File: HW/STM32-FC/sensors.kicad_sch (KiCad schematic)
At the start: 19 parts, among them J3 Molex 53048-03, U1 AMS1117-3.3, U5 BMP280, U7 BMI088, U8 LIS2MDLTR

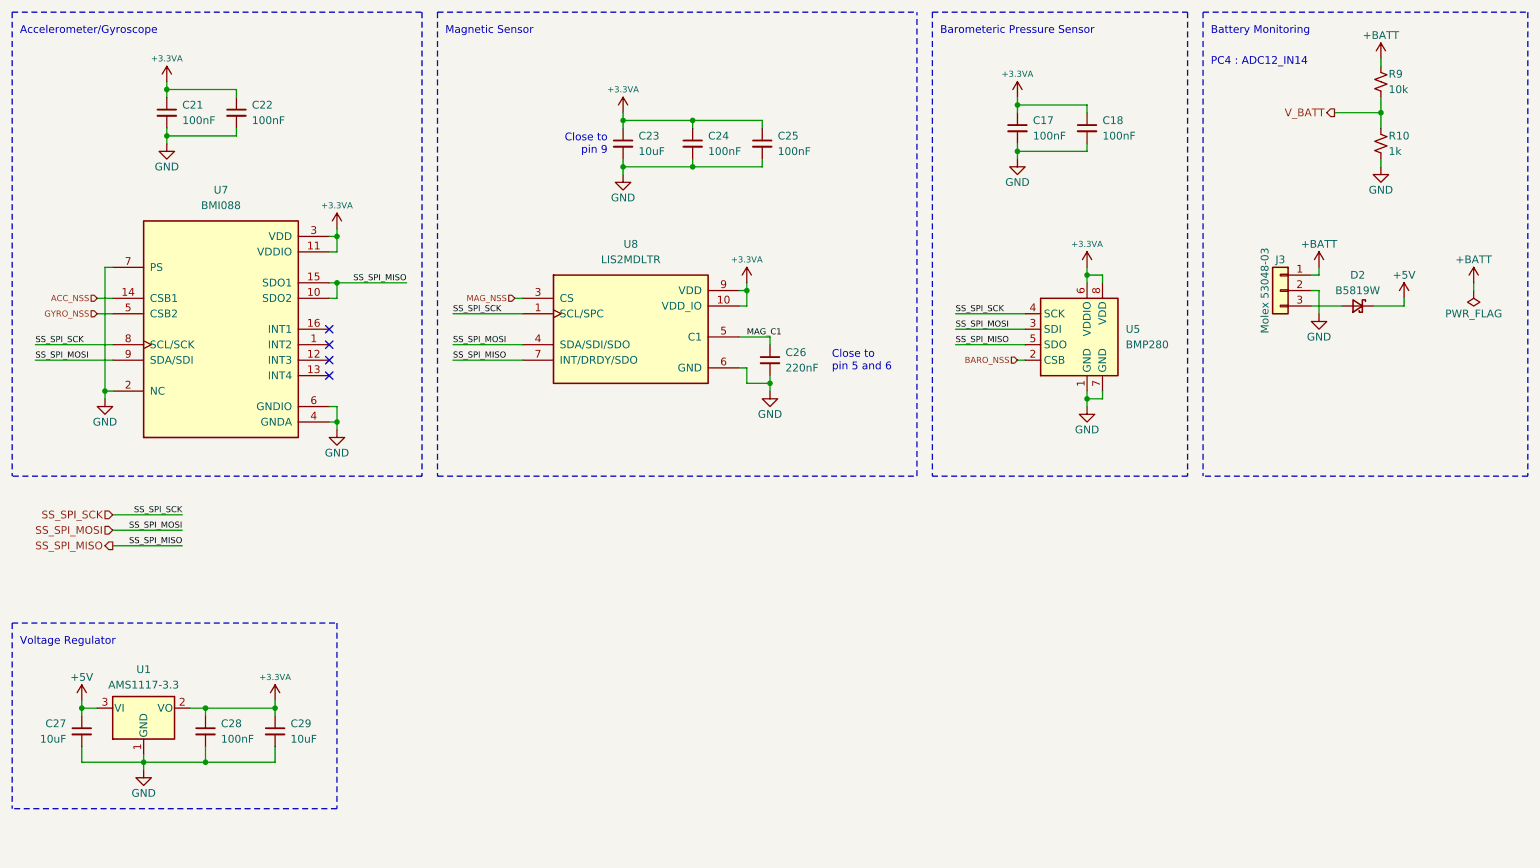
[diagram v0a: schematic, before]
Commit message: IMU update finished
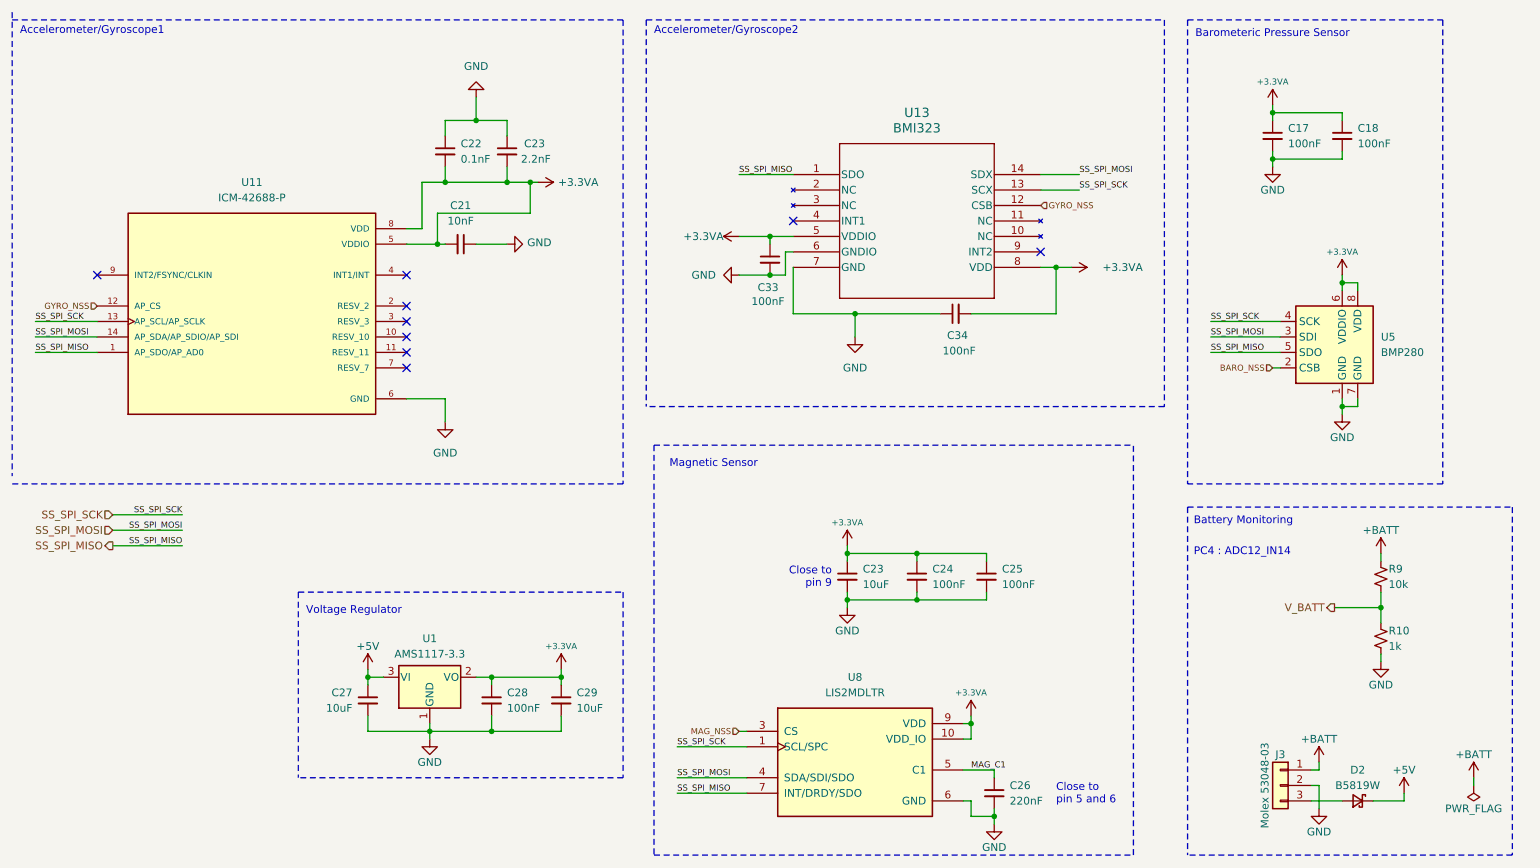
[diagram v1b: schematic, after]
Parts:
- removed U7: BMI088, Custom_Parts:PQFN50P450X300X100-16N, symbol BMI088:BMI088
- added C23: 2.2nF, Capacitor_SMD:C_0402_1005Metric, symbol Device:C_Small
- added C33, C34: 100nF, Capacitor_SMD:C_0402_1005Metric, symbol Device:C_Small
- added U11: ICM-42688-P, ICM-42688-P:PQFN50P300X250X97-14N, symbol ICM-42688-P:ICM-42688-P
- added U13: BMI323, BMI323_BOS, symbol BMI323:BMI323
- C21: value 100nF -> 10nF
- C22: value 100nF -> 0.1nF
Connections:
- net +3.3VA: now also C21.2, C22.2, C23.2, C33.1, C34.2, U11.5 (VDDIO), U11.8 (VDD), U13.5 (VDDIO), U13.8 (VDD); no longer C21.1, C22.1
- net GND: now also C21.1, C22.1, C23.1, C33.2, C34.1, U11.6 (GND), U13.6 (GNDIO), U13.7 (GND); no longer C21.2, C22.2
- net GYRO_NSS: now also U11.12 (AP_CS), U13.12 (CSB)
- net SS_SPI_MISO: now also U11.1 (AP_SDO/AP_AD0), U13.1 (SDO)
- net SS_SPI_MOSI: now also U11.14 (AP_SDA/AP_SDIO/AP_SDI), U13.14 (SDX)
- net SS_SPI_SCK: now also U11.13 (AP_SCL/AP_SCLK), U13.13 (SCX)
- no-connect marks 4 -> 9
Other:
- note added: "Accelerometer/Gyroscope1"
- note added: "Accelerometer/Gyroscope2"
- note removed: "Accelerometer/Gyroscope"
- moved on the sheet: C17, C18, C23, C24, C25, C26, C27, C28, C29, D2, J3, R10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
